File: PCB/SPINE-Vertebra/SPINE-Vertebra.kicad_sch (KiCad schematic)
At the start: 80 parts, among them J2 Conn_01x06, J4 Conn_01x06, Q1 NTMFS5C628NLT1G, Q2 NTMFS5C628NLT1G, Q3 NTMFS5C628NLT1G, Q4 NTMFS5C628NLT1G, Q7 VISHAY SI2309CDS-T1-GE3, Q8 Q_NMOS_GSD, U1 ACS724xLCTR-50AB, U2 LM74800QDRRRQ1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

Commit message: Finish Vertebra
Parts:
- removed C34, C41, C42, C43, C44, C45: 10uF, Capacitor_SMD:C_1206_3216Metric, symbol Device:C
- D1, D4, D5: value LED_Small -> LED
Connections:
- net +3.3V: now also C7.2, U3.8 (VCC)
- net +5V: no longer C7.2, U3.8 (VCC)
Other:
- note added: "CONNECTOR"
- note added: "LOW POWER"
- note added: "MOUNTING HOLE"
- note added: "RS485"
- moved on the sheet: C1, C10, C12, C13, C16, C17, C19, C2, C20, C21, C22, C25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

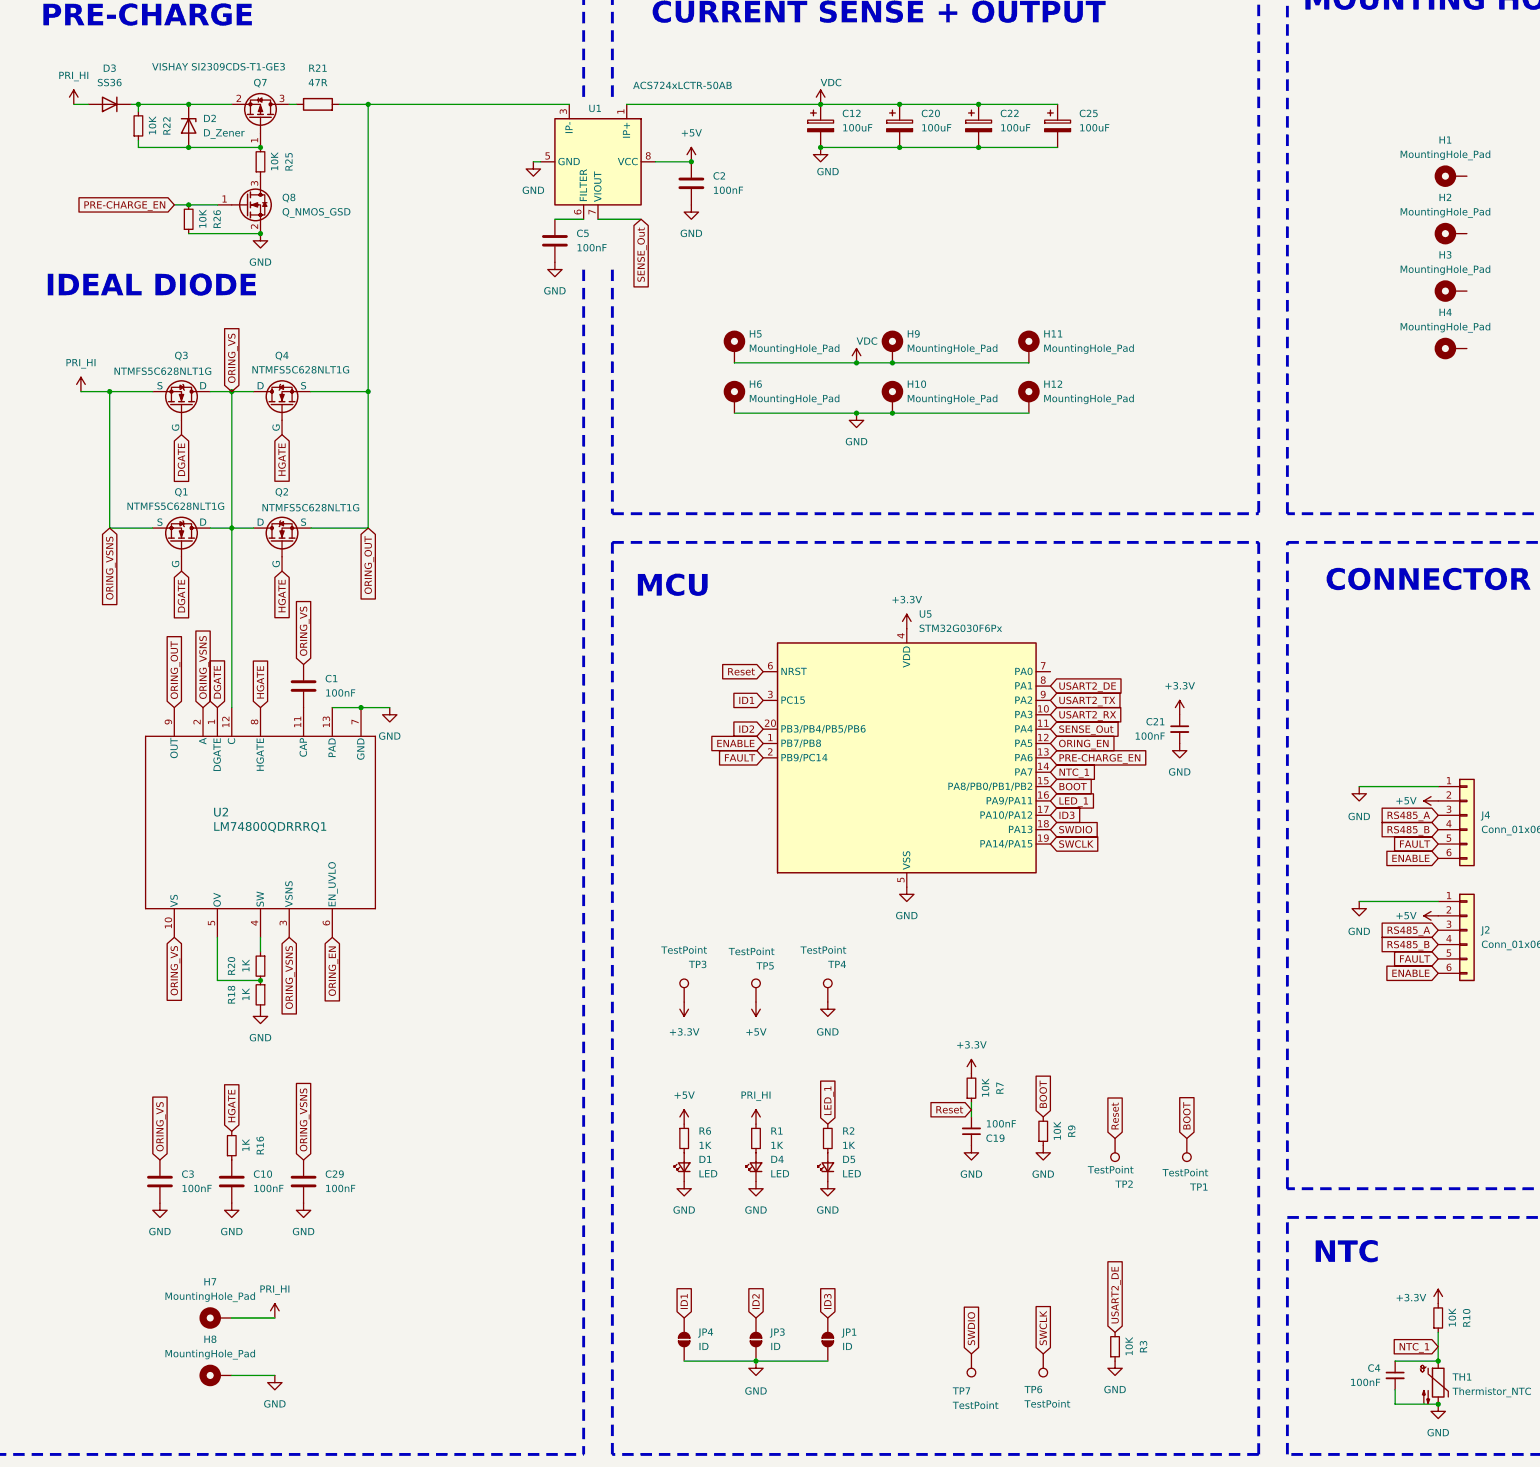
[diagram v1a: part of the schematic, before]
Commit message: Vertebra fix
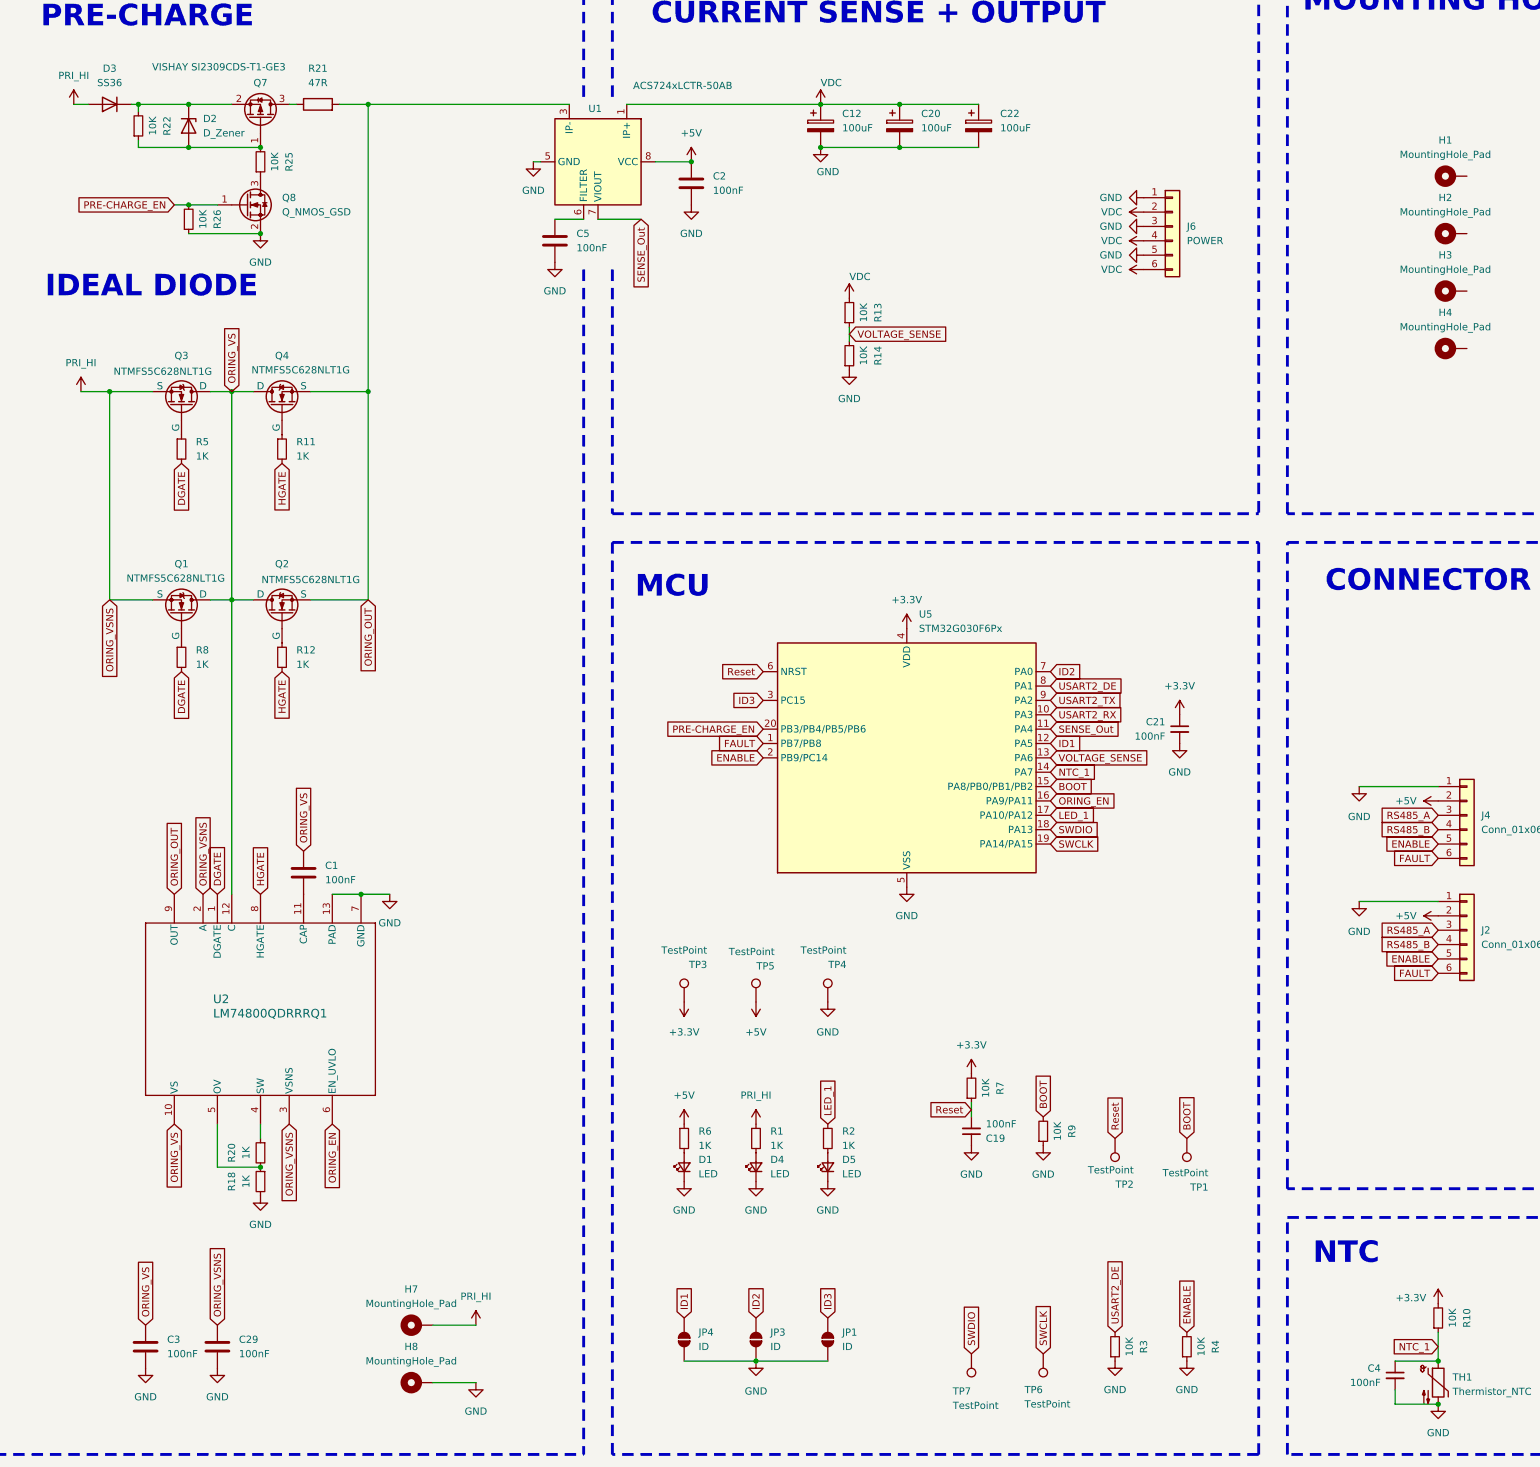
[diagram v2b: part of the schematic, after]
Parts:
- removed C10: 100nF, Capacitor_SMD:C_0603_1608Metric, symbol Device:C
- removed C25: 100uF, Capacitor_THT:CP_Radial_D10.0mm_P5.00mm, symbol Device:C_Polarized
- removed H10, H11, H12, H5, H6, H9: MountingHole_Pad, MountingHole:MountingHole_2.2mm_M2_Pad_Via, symbol Mechanical:MountingHole_Pad
- removed R16: 1K, Resistor_SMD:R_0603_1608Metric, symbol Device:R_Small
- added J6: POWER, TerminalBlock_MetzConnect:TerminalBlock_MetzConnect_Type094_RT03506HBLU_1x06_P5.00mm_Horizontal, symbol Connector_Generic:Conn_01x06
- added R11, R12, R5, R8: 1K, Resistor_SMD:R_0603_1608Metric, symbol Device:R_Small
- added R13, R14, R4: 10K, Resistor_SMD:R_0603_1608Metric, symbol Device:R_Small
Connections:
- net DGATE: now also R5.2, R8.2; no longer Q1.4 (G), Q3.4 (G)
- net ENABLE: now also J2.5 (Pin_5), J4.5 (Pin_5), U5.2 (PB9/PC14), R4.2; no longer J2.6 (Pin_6), J4.6 (Pin_6), U5.1 (PB7/PB8)
- net FAULT: now also J2.6 (Pin_6), J4.6 (Pin_6), U5.1 (PB7/PB8); no longer J2.5 (Pin_5), J4.5 (Pin_5), U5.2 (PB9/PC14)
- net GND: now also J6.1 (Pin_1), J6.3 (Pin_3), J6.5 (Pin_5), R14.1, R4.1
- net HGATE: now also R11.2, R12.2; no longer Q2.4 (G), Q4.4 (G)
- net ID1: now also U5.12 (PA5); no longer U5.3 (PC15)
- net ID2: now also U5.7 (PA0); no longer U5.20 (PB3/PB4/PB5/PB6)
- net ID3: now also U5.3 (PC15); no longer U5.17 (PA10/PA12)
- net LED_1: now also U5.17 (PA10/PA12); no longer U5.16 (PA9/PA11)
- net ORING_EN: now also U5.16 (PA9/PA11); no longer U5.12 (PA5)
- net PRE-CHARGE_EN: now also U5.20 (PB3/PB4/PB5/PB6); no longer U5.13 (PA6)
- net VDC: now also J6.2 (Pin_2), J6.4 (Pin_4), J6.6 (Pin_6), R13.2
- new net: Q4.4 (G), R11.1
- new net: Q3.4 (G), R5.1
- new net: Q2.4 (G), R12.1
- new net: Q1.4 (G), R8.1
- new net VOLTAGE_SENSE: R13.1, R14.2, U5.13 (PA6)
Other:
- moved on the sheet: C1, C29, C3, H7, H8, Q1, Q2, R18, R20, U2

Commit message: update
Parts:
- removed D5: LED, LED_SMD:LED_0603_1608Metric, symbol Device:LED_Small
- removed R2: 1K, Resistor_SMD:R_0603_1608Metric, symbol Device:R_Small
- added D6: WS2812B-2020, LED_SMD:LED_WS2812B-2020_PLCC4_2.0x2.0mm, symbol LED:WS2812B-2020
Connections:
- net +5V: now also D6.4 (VDD)
- net BOOT: now also D6.3 (DIN)
- net GND: now also D6.2 (VSS)
- net ID1: now also U5.13 (PA6); no longer U5.12 (PA5)
- net VOLTAGE_SENSE: now also U5.12 (PA5); no longer U5.13 (PA6)
- net LED_1: no longer names the net of U5.17 (PA10/PA12)
- net SENSE_Out renamed CURRENT_SENSE

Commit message: update
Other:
- moved on the sheet: C13, C16, C17, D6, U4
